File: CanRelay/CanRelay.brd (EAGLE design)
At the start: 93 x 67.9 mm, 23 parts

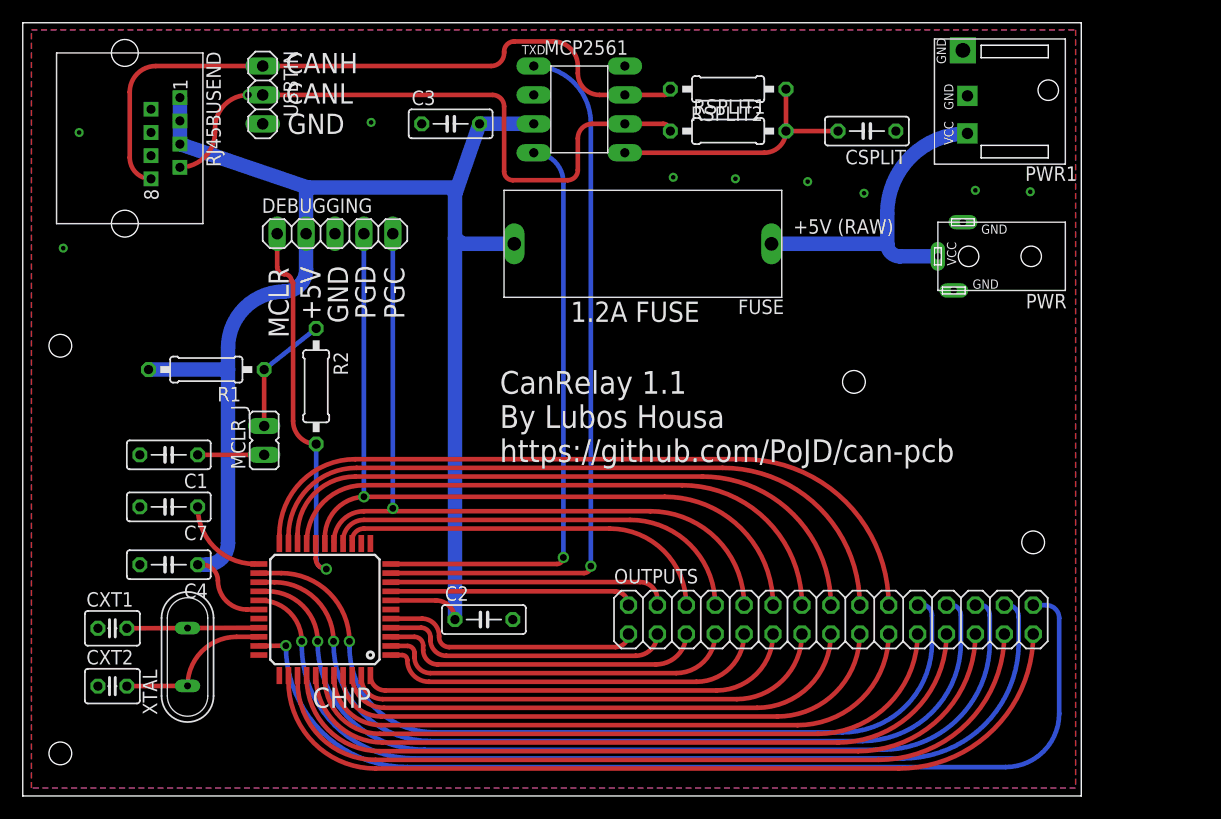
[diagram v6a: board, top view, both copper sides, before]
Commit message: #19 final changes after new chip  - added labels to the output pinheader  - added new cutout areas in top copper near the output pinheader to  avoid ground copper antenna fingers in there  - rewired MCLR components and created more space for all capacitor so  that they all can hopefully be laid down  - +5V rewired close to MCLR pin too so that it is nicer
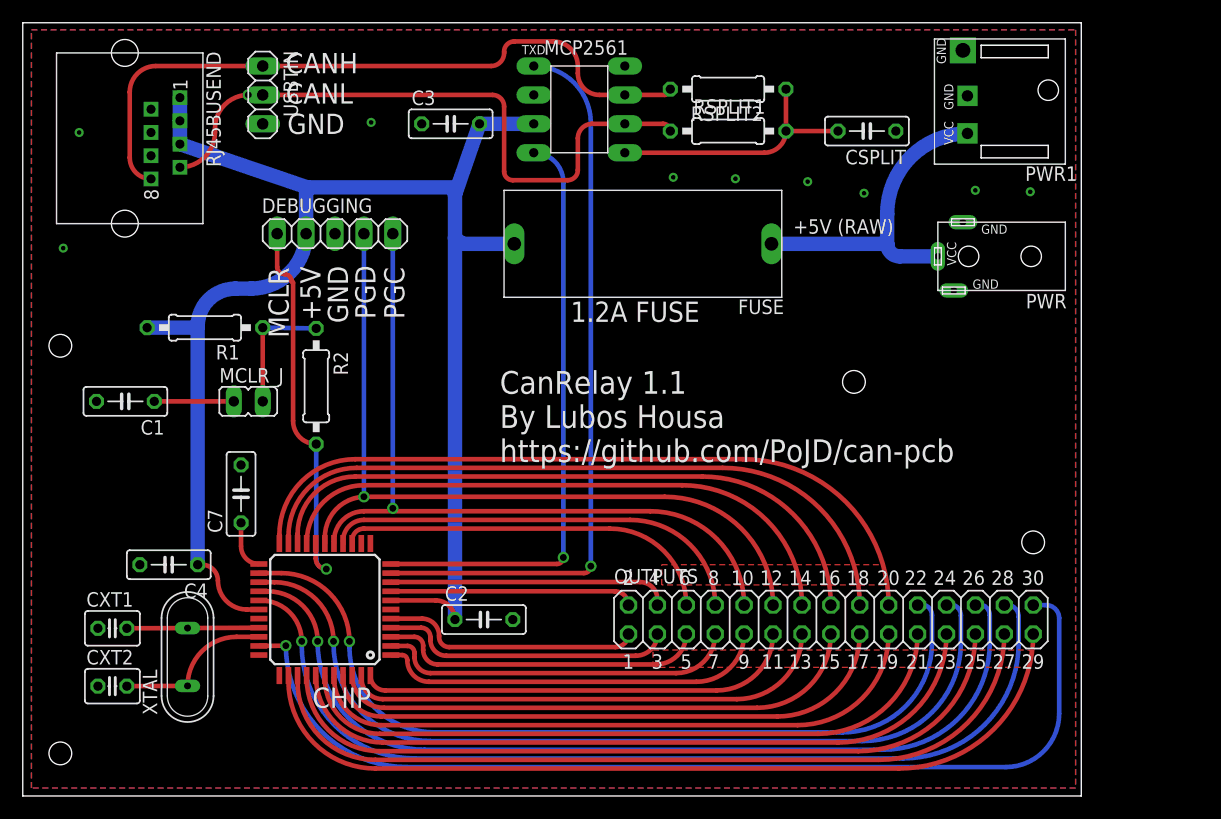
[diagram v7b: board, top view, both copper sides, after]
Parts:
- moved C7 6.45 mm to (19.2, 26.5), turned to 90 degrees
- moved C1 6.05 mm to (9.02, 34.7)
- moved MCLR_J 3.70 mm to (19.8, 34.7), turned to 270 degrees
- moved R1 3.69 mm to (16.0, 41.1)
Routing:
- net ENVREG: track 7.45 -> 4.27 mm
- net +5V: track 141.5 -> 139.4 mm
- net N$1: track 5.84 -> 6.99 mm
- added copper zone on layer 1, net N$3
- added copper zone on layer 1, net SKIP2
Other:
- board text added: "1"
- board text added: "10"
- board text added: "11"
- board text added: "12"
- board text added: "13"
- board text added: "14"
- board text added: "15"
- board text added: "16"
- board text added: "17"
- board text added: "18"
- board text added: "19"
- board text added: "2"
- board text added: "20"
- board text added: "21"
- board text added: "22"
- board text added: "23"
- board text added: "24"
- board text added: "25"
- board text added: "26"
- board text added: "27"
- board text added: "28"
- board text added: "29"
- board text added: "3"
- board text added: "30"
- board text added: "4"
- board text added: "5"
- board text added: "6"
- board text added: "7"
- board text added: "8"
- board text added: "9"
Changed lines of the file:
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@@
 <hole x="3.302" y="3.742" drill="2"/>
 <hole x="73.025" y="36.381" drill="2"/>
+<text x="52.705" y="11.176" size="1.27" layer="21">1</text>
+<text x="55.245" y="11.176" size="1.27" layer="21">3</text>
+<text x="57.785" y="11.176" size="1.27" layer="21">5</text>
+<text x="60.198" y="11.176" size="1.27" layer="21">7</text>
+<text x="62.865" y="11.176" size="1.27" layer="21">9</text>
+<text x="64.897" y="11.176" size="1.27" layer="21">11</text>
+<text x="67.31" y="11.176" size="1.27" layer="21">13</text>
+<text x="69.85" y="11.176" size="1.27" layer="21">15</text>
+<text x="72.39" y="11.176" size="1.27" layer="21">17</text>
+<text x="74.93" y="11.176" size="1.27" layer="21">19</text>
+<text x="77.597" y="11.176" size="1.27" layer="21">21</text>
+<text x="80.01" y="11.176" size="1.27" layer="21">23</text>
+<text x="82.677" y="11.176" size="1.27" layer="21">25</text>
+<text x="85.217" y="11.176" size="1.27" layer="21">27</text>
+<text x="87.757" y="11.176" size="1.27" layer="21">29</text>
+<text x="52.705" y="18.542" size="1.27" layer="21">2</text>
+<text x="54.991" y="18.542" size="1.27" layer="21">4</text>
+<text x="57.658" y="18.542" size="1.27" layer="21">6</text>
+<text x="60.198" y="18.542" size="1.27" layer="21">8</text>
+<text x="62.23" y="18.542" size="1.27" layer="21">10</text>
+<text x="64.77" y="18.542" size="1.27" layer="21">12</text>
+<text x="67.31" y="18.542" size="1.27" layer="21">14</text>
+<text x="69.85" y="18.542" size="1.27" layer="21">16</text>
+<text x="72.39" y="18.542" size="1.27" layer="21">18</text>
+<text x="75.057" y="18.542" size="1.27" layer="21">20</text>
+<text x="77.47" y="18.542" size="1.27" layer="21">22</text>
+<text x="80.01" y="18.542" size="1.27" layer="21">24</text>
+<text x="82.55" y="18.542" size="1.27" layer="21">26</text>
+<text x="85.09" y="18.542" size="1.27" layer="21">28</text>
+<text x="87.757" y="18.542" size="1.27" layer="21">30</text>
 </plain>
 <attributes>
@@
 </autorouter>
 <elements>
-<element name="C1" library="rcl" package="C050-025X075" value="0.1uF" x="12.827" y="29.972" rot="R180"/>
+<element name="C1" library="rcl" package="C050-025X075" value="0.1uF" x="9.017" y="34.671" rot="R180"/>
 <element name="C2" library="rcl" package="C050-025X075" value="0.1uF" x="40.513" y="15.5"/>
 <element name="C3" library="rcl" package="C050-025X075" value="0.1uF" x="37.592" y="59.055"/>
-<element name="C7" library="rcl" package="C050-025X075" value="10 uF" x="12.827" y="25.4" rot="R180"/>
+<element name="C7" library="rcl" package="C050-025X075" value="10 uF" x="19.177" y="26.543" rot="R90"/>
 <element name="CSPLIT" library="rcl" package="C050-025X075" value="4.7nF" x="74.168" y="58.42" rot="R180"/>
 <element name="CXT1" library="rcl" package="C025-030X050" value="33pF" x="7.874" y="14.732"/>
 <element name="CXT2" library="rcl" package="C025-030X050" value="33pF" x="7.874" y="9.652"/>
 <element name="DEBUGGING" library="pinhead" package="1X05" value="" x="27.432" y="49.403"/>
-<element name="MCLR_J" library="jumper" package="JP1" value="" x="21.209" y="31.242"/>
+<element name="MCLR_J" library="jumper" package="JP1" value="" x="19.812" y="34.671" rot="R270"/>
 <element name="MCP2561" library="PoJD" package="MCP2561_PDIP" value="MCP2561MCP" x="48.895" y="60.325"/>
 <element name="PWR" library="PoJD" package="DC-JACK-GK0.65" value="DC-JACK-GK0.65S" x="86" y="47.413" rot="R180"/>
-<element name="R1" library="rcl" package="0207/10" value="10000" x="16.129" y="37.465" rot="R180"/>
+<element name="R1" library="rcl" package="0207/10" value="10000" x="16.002" y="41.148" rot="R180"/>
 <element name="R2" library="rcl" package="0207/10" value="470" x="25.781" y="36" rot="R270"/>
 <element name="RJ45BUSEND" library="PoJD" package="WEBP88_RJ45_SINGLE" value="WEBP88_SSINGLE" x="9.398" y="57.785" rot="R270"/>
@@
 <wire x1="32.343" y1="17.183" x2="36.29" y2="17.183" width="0.4064" layer="1"/>
 <wire x1="36.29" y1="17.183" x2="37.973" y2="15.5" width="0.4064" layer="1" curve="-90"/>
-<wire x1="15.367" y1="20.32" x2="16.129" y2="20.32" width="1.27" layer="16"/>
-<wire x1="16.129" y1="20.32" x2="18.034" y2="22.225" width="1.27" layer="16" curve="90"/>
-<wire x1="18.034" y1="22.225" x2="18.034" y2="37.465" width="1.27" layer="16"/>
-<wire x1="18.034" y1="37.465" x2="18.034" y2="39.37" width="1.27" layer="16"/>
-<wire x1="18.034" y1="39.37" x2="22.987" y2="44.323" width="1.27" layer="16" curve="-90"/>
-<wire x1="22.987" y1="44.323" x2="24.892" y2="46.228" width="1.27" layer="16" curve="90"/>
-<wire x1="24.892" y1="46.228" x2="24.892" y2="49.403" width="1.27" layer="16"/>
-<wire x1="11.049" y1="37.465" x2="18.034" y2="37.465" width="1.27" layer="16"/>
+<wire x1="24.892" y1="49.403" x2="20.066" y2="44.577" width="1.27" layer="16" curve="-90"/>
+<wire x1="20.066" y1="44.577" x2="18.669" y2="44.577" width="1.27" layer="16"/>
+<wire x1="18.669" y1="44.577" x2="15.367" y2="41.275" width="1.27" layer="16" curve="90"/>
+<wire x1="15.367" y1="41.275" x2="15.367" y2="20.32" width="1.27" layer="16"/>
+<wire x1="15.367" y1="41.275" x2="15.24" y2="41.148" width="1.27" layer="16" curve="-90"/>
+<wire x1="15.24" y1="41.148" x2="10.922" y2="41.148" width="1.27" layer="16"/>
 </signal>
 <signal name="GND">
@@
 <contactref element="MCLR_J" pad="2"/>
 <contactref element="R2" pad="1"/>
-<wire x1="21.209" y1="32.512" x2="21.209" y2="37.465" width="0.4064" layer="1"/>
-<wire x1="21.209" y1="37.465" x2="25.781" y2="41.08" width="0.4064" layer="16"/>
+<wire x1="21.082" y1="34.671" x2="21.082" y2="41.148" width="0.4064" layer="1"/>
+<wire x1="21.082" y1="41.148" x2="25.781" y2="41.08" width="0.4064" layer="16"/>
 </signal>
 <signal name="MCLR">
@@
 <contactref element="C1" pad="1"/>
 <contactref element="MCLR_J" pad="1"/>
-<wire x1="15.367" y1="29.972" x2="21.209" y2="29.972" width="0.4064" layer="1"/>
+<wire x1="11.557" y1="34.671" x2="18.542" y2="34.671" width="0.4064" layer="1"/>
 </signal>
 <signal name="OSC1">
@@
 <contactref element="C7" pad="1"/>
 <contactref element="CHIP" pad="23"/>
-<wire x1="20.743" y1="20.383" x2="20.384" y2="20.383" width="0.4064" layer="1"/>
-<wire x1="20.384" y1="20.383" x2="15.367" y2="25.4" width="0.4064" layer="1" curve="-90"/>
+<wire x1="20.743" y1="20.383" x2="19.177" y2="21.949" width="0.4064" layer="1" curve="-90"/>
+<wire x1="19.177" y1="21.949" x2="19.177" y2="24.003" width="0.4064" layer="1"/>
 </signal>
 <signal name="O1">
@@
 <wire x1="29.972" y1="26.289" x2="29.972" y2="49.403" width="0.4064" layer="16"/>
 </signal>
+<signal name="N$3">
+<polygon width="0.4064" layer="1" pour="cutout">
+<vertex x="56.134" y="20.32"/>
+<vertex x="75.692" y="20.32"/>
+<vertex x="75.692" y="20.447"/>
+<vertex x="75.692" y="18.542"/>
+<vertex x="56.134" y="18.542"/>
+</polygon>
+</signal>
+<signal name="SKIP2">
+<polygon width="0.4064" layer="1" pour="cutout">
+<vertex x="55.372" y="12.827"/>
+<vertex x="88.519" y="12.827"/>
+<vertex x="88.519" y="11.303"/>
+<vertex x="55.372" y="11.303"/>
+</polygon>
+</signal>
 </signals>
